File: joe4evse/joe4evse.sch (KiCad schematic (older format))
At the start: 39 parts, among them J1 USB_B_Micro, J10 Conn_01x02, J11 Conn_01x02, J2 Conn_01x03, J3 Conn_01x03, J4 Conn_01x02, J5 Conn_01x03, J6 CONNFLY_Elec_DS1129-04-S8B0P-X, J7 8P8C_LED_Shielded, J9 Conn_01x02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

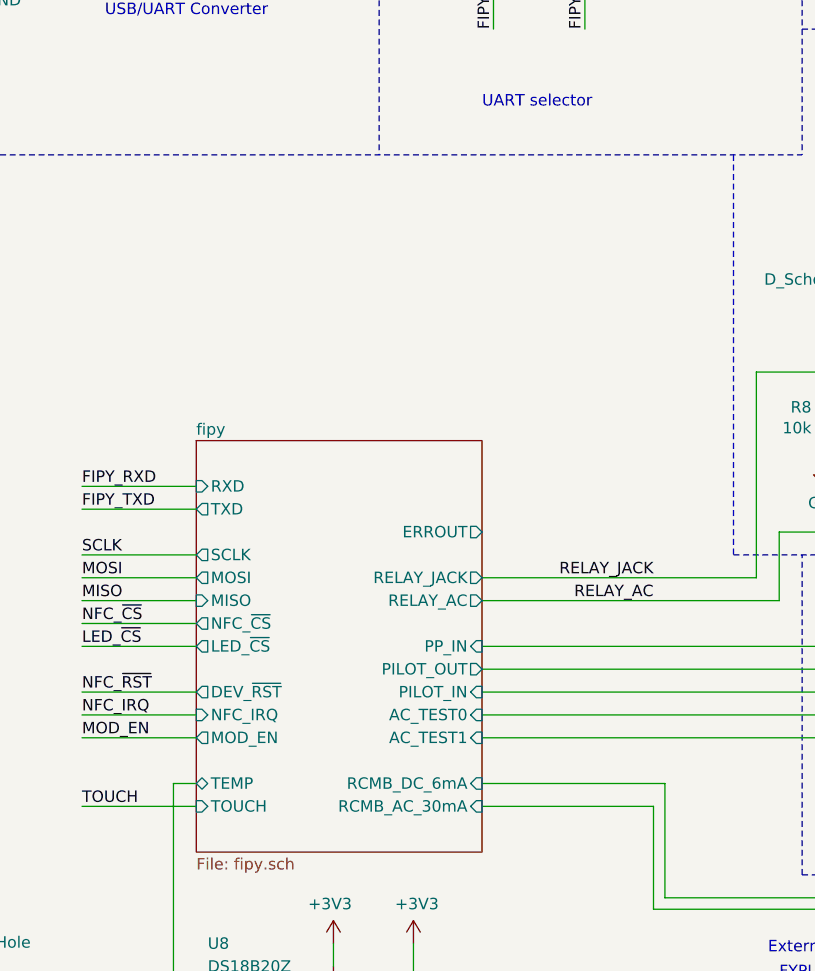
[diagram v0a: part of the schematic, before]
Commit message: joe/*: Add 0.1" header for easy access to RJ45 signals
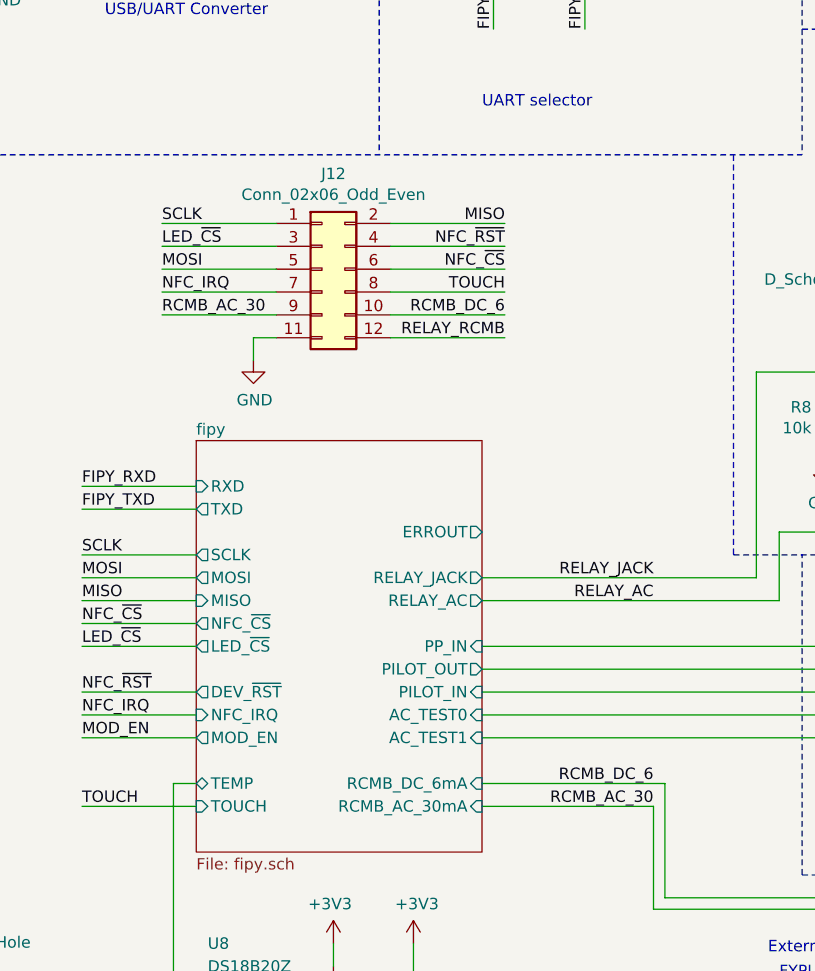
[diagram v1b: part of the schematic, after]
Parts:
- added J12: Conn_02x06_Odd_Even, Connector_PinHeader_2.54mm:PinHeader_2x06_P2.54mm_Vertical, symbol Connector_Generic:Conn_02x06_Odd_Even
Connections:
- net GND: now also J12.11 (Pin_11)
- net LED_~CS: now also J12.3 (Pin_3)
- net MISO: now also J12.2 (Pin_2)
- net MOSI: now also J12.5 (Pin_5)
- net NFC_IRQ: now also J12.7 (Pin_7)
- net NFC_~CS: now also J12.6 (Pin_6)
- net NFC_~RST: now also J12.4 (Pin_4)
- net RELAY_RCMB: now also J12.12 (Pin_12)
- net SCLK: now also J12.1 (Pin_1)
- net TOUCH: now also J12.8 (Pin_8)
- net fipy/RCMB_AC_30mA renamed RCMB_AC_30
- net RCMB_AC_30: now also J12.9 (Pin_9)
- net fipy/RCMB_DC_6mA renamed RCMB_DC_6
- net RCMB_DC_6: now also J12.10 (Pin_10)
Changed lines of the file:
@@
 Wire Wire Line
 	5450 7100 5450 7400
+$Comp
+L Connector_Generic:Conn_02x06_Odd_Even J12
+U 1 1 5DFFDDFE
+P 5050 3650
+F 0 "J12" H 5100 4067 50  0000 C CNN
+F 1 "Conn_02x06_Odd_Even" H 5100 3976 50  0000 C CNN
+F 2 "Connector_PinHeader_2.54mm:PinHeader_2x06_P2.54mm_Vertical" H 5050 3650 50  0001 C CNN
+F 3 "~" H 5050 3650 50  0001 C CNN
+	1    5050 3650
+	1    0    0    -1
+$EndComp
+Wire Wire Line
+	4850 3750 4350 3750
+Wire Wire Line
+	5350 3550 5850 3550
+Wire Wire Line
+	4850 3550 4350 3550
+Wire Wire Line
+	5350 3650 5850 3650
+Wire Wire Line
+	4850 3650 4350 3650
+Wire Wire Line
+	5350 3450 5850 3450
+Wire Wire Line
+	4850 3450 4350 3450
+Text Label 4350 3450 0    50   ~ 0
+SCLK
+Text Label 5850 3450 2    50   ~ 0
+MISO
+Text Label 4350 3650 0    50   ~ 0
+MOSI
+Text Label 5850 3650 2    50   ~ 0
+NFC_~CS
+Text Label 4350 3550 0    50   ~ 0
+LED_~CS
+Text Label 5850 3550 2    50   ~ 0
+NFC_~RST
+Text Label 4350 3750 0    50   ~ 0
+NFC_IRQ
+Text Label 5850 3750 2    50   ~ 0
+TOUCH
+Wire Wire Line
+	5350 3750 5850 3750
+Text Label 6500 6000 2    50   ~ 0
+RCMB_AC_30
+Text Label 6500 5900 2    50   ~ 0
+RCMB_DC_6
+Wire Wire Line
+	4850 3850 4350 3850
+Wire Wire Line
+	5350 3850 5850 3850
+Text Label 4350 3850 0    50   ~ 0
+RCMB_AC_30
+Text Label 5850 3850 2    50   ~ 0
+RCMB_DC_6
+Text Label 5850 3950 2    50   ~ 0
+RELAY_RCMB
+Wire Wire Line
+	5850 3950 5350 3950
+$Comp
+L power:GND #PWR075
+U 1 1 5E0BB16B
+P 4750 4050
+AR Path="/5E0BB16B" Ref="#PWR075"  Part="1"
+AR Path="/5E295EB5/5E0BB16B" Ref="#PWR?"  Part="1"
+AR Path="/5E2A129E/5E0BB16B" Ref="#PWR?"  Part="1"
+AR Path="/5E2A9DD8/5E0BB16B" Ref="#PWR?"  Part="1"
+F 0 "#PWR075" H 4750 3800 50  0001 C CNN
+F 1 "GND" H 4755 3877 50  0000 C CNN
+F 2 "" H 4750 4050 50  0001 C CNN
+F 3 "" H 4750 4050 50  0001 C CNN
+	1    4750 4050
+	1    0    0    -1
+$EndComp
+Wire Wire Line
+	4750 4050 4750 3950
+Wire Wire Line
+	4750 3950 4850 3950
 $EndSCHEMATC

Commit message: joe/pcb: Misc silk fixes
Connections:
- net MOD_A: now reaches J2.3 (Pin_3), U2.6 (A)
- net MOD_B: now reaches J2.1 (Pin_1), U2.7 (B)
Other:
- moved on the sheet: J2
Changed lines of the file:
@@
 L power:GND #PWR014
 U 1 1 5D2C078F
-P 9650 2300
-F 0 "#PWR014" H 9650 2050 50  0001 C CNN
-F 1 "GND" H 9655 2127 50  0000 C CNN
-F 2 "" H 9650 2300 50  0001 C CNN
-F 3 "" H 9650 2300 50  0001 C CNN
-	1    9650 2300
+P 9900 2300
+F 0 "#PWR014" H 9900 2050 50  0001 C CNN
+F 1 "GND" H 9905 2127 50  0000 C CNN
+F 2 "" H 9900 2300 50  0001 C CNN
+F 3 "" H 9900 2300 50  0001 C CNN
+	1    9900 2300
 	1    0    0    -1
 $EndComp
@@
 	9550 1800 9550 1750
 Wire Wire Line
-	9550 1750 9750 1750
+	9550 1750 10000 1750
 Wire Wire Line
 	9450 1500 9550 1500
@@
 	9550 1500 9550 1550
 Wire Wire Line
-	9550 1550 9750 1550
-Wire Wire Line
-	9650 2300 9650 1650
-Wire Wire Line
-	9650 1650 9750 1650
+	9550 1550 10000 1550
 $Comp
 L power:+3V3 #PWR03
@@
 Text Label 6300 950  3    50   ~ 0
 MOD_RX
-$Comp
-L Connector_Generic:Conn_01x03 J2
-U 1 1 5E290D0B
-P 9950 1650
-F 0 "J2" H 10030 1692 50  0000 L CNN
-F 1 "Conn_01x03" H 10030 1601 50  0000 L CNN
-F 2 "Connector_JST:JST_PH_B3B-PH-K_1x03_P2.00mm_Vertical" H 9950 1650 50  0001 C CNN
-F 3 "~" H 9950 1650 50  0001 C CNN
-	1    9950 1650
-	1    0    0    -1
-$EndComp
 Wire Wire Line
 	8950 4500 8950 4300
@@
 Wire Wire Line
 	4750 3950 4850 3950
+Text Label 9550 1550 0    50   ~ 0
+MOD_B
+Text Label 9550 1750 0    50   ~ 0
+MOD_A
+$Comp
+L Connector_Generic:Conn_01x03 J2
+U 1 1 5E290D0B
+P 10200 1650
+F 0 "J2" H 10280 1692 50  0000 L CNN
+F 1 "Conn_01x03" H 10280 1601 50  0000 L CNN
+F 2 "Connector_JST:JST_PH_B3B-PH-K_1x03_P2.00mm_Vertical" H 10200 1650 50  0001 C CNN
+F 3 "~" H 10200 1650 50  0001 C CNN
+	1    10200 1650
+	1    0    0    -1
+$EndComp
+Wire Wire Line
+	10000 1650 9900 1650
+Wire Wire Line
+	9900 1650 9900 2300
 $EndSCHEMATC

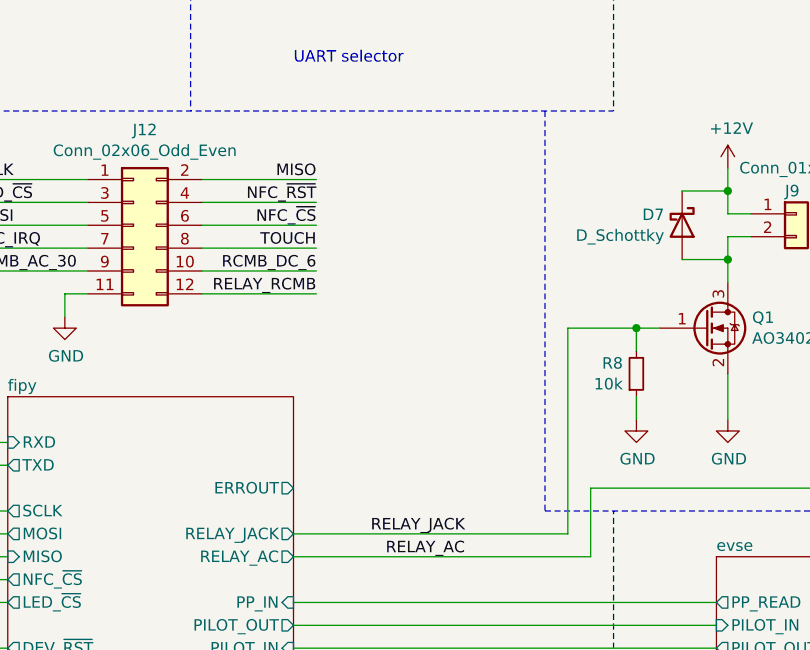
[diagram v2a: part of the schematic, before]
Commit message: joe: Add 12V ERROUT
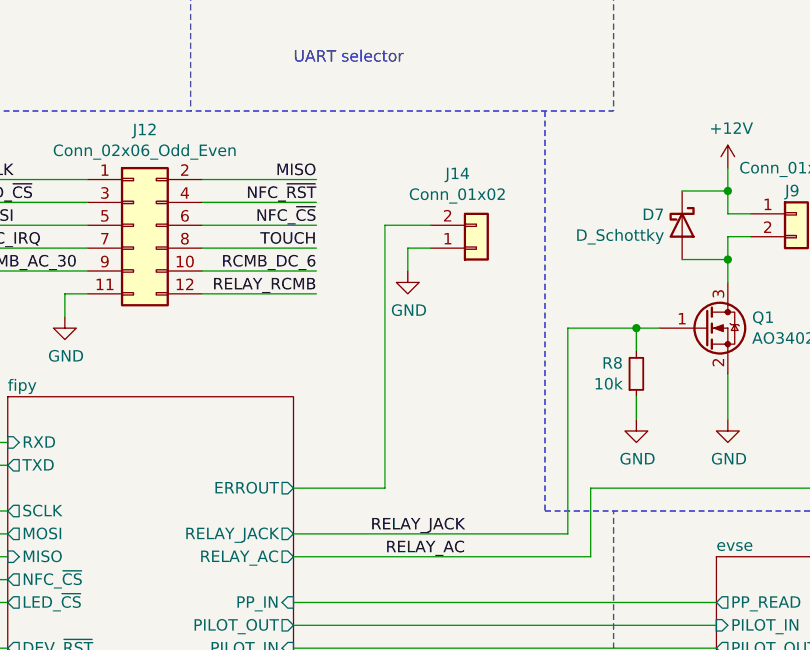
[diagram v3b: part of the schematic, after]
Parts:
- added J14: Conn_01x02, Connector_JST:JST_PH_B2B-PH-K_1x02_P2.00mm_Vertical, symbol Connector_Generic:Conn_01x02
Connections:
- net GND: now also J14.1 (Pin_1)
- net fipy/ERROUT: now also J14.2 (Pin_2)
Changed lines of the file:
@@
 Wire Wire Line
 	5450 7100 5450 7400
-$Comp
-L Connector_Generic:Conn_02x06_Odd_Even J12
-U 1 1 5DFFDDFE
-P 5050 3650
-F 0 "J12" H 5100 4067 50  0000 C CNN
-F 1 "Conn_02x06_Odd_Even" H 5100 3976 50  0000 C CNN
-F 2 "Connector_PinHeader_2.54mm:PinHeader_2x06_P2.54mm_Vertical" H 5050 3650 50  0001 C CNN
-F 3 "~" H 5050 3650 50  0001 C CNN
-	1    5050 3650
-	1    0    0    -1
-$EndComp
-Wire Wire Line
-	4850 3750 4350 3750
-Wire Wire Line
-	5350 3550 5850 3550
-Wire Wire Line
-	4850 3550 4350 3550
-Wire Wire Line
-	5350 3650 5850 3650
-Wire Wire Line
-	4850 3650 4350 3650
-Wire Wire Line
-	5350 3450 5850 3450
-Wire Wire Line
-	4850 3450 4350 3450
-Text Label 4350 3450 0    50   ~ 0
-SCLK
-Text Label 5850 3450 2    50   ~ 0
-MISO
-Text Label 4350 3650 0    50   ~ 0
-MOSI
-Text Label 5850 3650 2    50   ~ 0
-NFC_~CS
-Text Label 4350 3550 0    50   ~ 0
-LED_~CS
-Text Label 5850 3550 2    50   ~ 0
-NFC_~RST
-Text Label 4350 3750 0    50   ~ 0
-NFC_IRQ
-Text Label 5850 3750 2    50   ~ 0
-TOUCH
-Wire Wire Line
-	5350 3750 5850 3750
 Text Label 6500 6000 2    50   ~ 0
 RCMB_AC_30
 Text Label 6500 5900 2    50   ~ 0
 RCMB_DC_6
-Wire Wire Line
-	4850 3850 4350 3850
-Wire Wire Line
-	5350 3850 5850 3850
-Text Label 4350 3850 0    50   ~ 0
-RCMB_AC_30
-Text Label 5850 3850 2    50   ~ 0
-RCMB_DC_6
-Text Label 5850 3950 2    50   ~ 0
-RELAY_RCMB
-Wire Wire Line
-	5850 3950 5350 3950
-$Comp
-L power:GND #PWR075
-U 1 1 5E0BB16B
-P 4750 4050
-AR Path="/5E0BB16B" Ref="#PWR075"  Part="1"
-AR Path="/5E295EB5/5E0BB16B" Ref="#PWR?"  Part="1"
-AR Path="/5E2A129E/5E0BB16B" Ref="#PWR?"  Part="1"
-AR Path="/5E2A9DD8/5E0BB16B" Ref="#PWR?"  Part="1"
-F 0 "#PWR075" H 4750 3800 50  0001 C CNN
-F 1 "GND" H 4755 3877 50  0000 C CNN
-F 2 "" H 4750 4050 50  0001 C CNN
-F 3 "" H 4750 4050 50  0001 C CNN
-	1    4750 4050
-	1    0    0    -1
-$EndComp
-Wire Wire Line
-	4750 4050 4750 3950
-Wire Wire Line
-	4750 3950 4850 3950
 Text Label 9550 1550 0    50   ~ 0
 MOD_B
@@
 Wire Wire Line
 	9900 1650 9900 2300
+Wire Wire Line
+	4750 3950 4850 3950
+Wire Wire Line
+	4750 4050 4750 3950
+$Comp
+L power:GND #PWR075
+U 1 1 5E0BB16B
+P 4750 4050
+AR Path="/5E0BB16B" Ref="#PWR075"  Part="1"
+AR Path="/5E295EB5/5E0BB16B" Ref="#PWR?"  Part="1"
+AR Path="/5E2A129E/5E0BB16B" Ref="#PWR?"  Part="1"
+AR Path="/5E2A9DD8/5E0BB16B" Ref="#PWR?"  Part="1"
+F 0 "#PWR075" H 4750 3800 50  0001 C CNN
+F 1 "GND" H 4755 3877 50  0000 C CNN
+F 2 "" H 4750 4050 50  0001 C CNN
+F 3 "" H 4750 4050 50  0001 C CNN
+	1    4750 4050
+	1    0    0    -1
+$EndComp
+Wire Wire Line
+	5850 3950 5350 3950
+Text Label 5850 3950 2    50   ~ 0
+RELAY_RCMB
+Text Label 5850 3850 2    50   ~ 0
+RCMB_DC_6
+Text Label 4350 3850 0    50   ~ 0
+RCMB_AC_30
+Wire Wire Line
+	5350 3850 5850 3850
+Wire Wire Line
+	4850 3850 4350 3850
+Wire Wire Line
+	5350 3750 5850 3750
+Text Label 5850 3750 2    50   ~ 0
+TOUCH
+Text Label 4350 3750 0    50   ~ 0
+NFC_IRQ
+Text Label 5850 3550 2    50   ~ 0
+NFC_~RST
+Text Label 4350 3550 0    50   ~ 0
+LED_~CS
+Text Label 5850 3650 2    50   ~ 0
+NFC_~CS
+Text Label 4350 3650 0    50   ~ 0
+MOSI
+Text Label 5850 3450 2    50   ~ 0
+MISO
+Text Label 4350 3450 0    50   ~ 0
+SCLK
+Wire Wire Line
+	4850 3450 4350 3450
+Wire Wire Line
+	5350 3450 5850 3450
+Wire Wire Line
+	4850 3650 4350 3650
+Wire Wire Line
+	5350 3650 5850 3650
+Wire Wire Line
+	4850 3550 4350 3550
+Wire Wire Line
+	5350 3550 5850 3550
+Wire Wire Line
+	4850 3750 4350 3750
+$Comp
+L Connector_Generic:Conn_02x06_Odd_Even J12
+U 1 1 5DFFDDFE
+P 5050 3650
+F 0 "J12" H 5100 4067 50  0000 C CNN
+F 1 "Conn_02x06_Odd_Even" H 5100 3976 50  0000 C CNN
+F 2 "Connector_PinHeader_2.54mm:PinHeader_2x06_P2.54mm_Vertical" H 5050 3650 50  0001 C CNN
+F 3 "~" H 5050 3650 50  0001 C CNN
+	1    5050 3650
+	1    0    0    -1
+$EndComp
+$Comp
+L Connector_Generic:Conn_01x02 J14
+U 1 1 5E66DC84
+P 6550 3750
+F 0 "J14" H 6468 3425 50  0000 C CNN
+F 1 "Conn_01x02" H 6468 3516 50  0000 C CNN
+F 2 "Connector_JST:JST_PH_B2B-PH-K_1x02_P2.00mm_Vertical" H 6550 3750 50  0001 C CNN
+F 3 "~" H 6550 3750 50  0001 C CNN
+	1    6550 3750
+	1    0    0    1
+$EndComp
+$Comp
+L power:GND #PWR081
+U 1 1 5E66E81F
+P 6250 3850
+AR Path="/5E66E81F" Ref="#PWR081"  Part="1"
+AR Path="/5E295EB5/5E66E81F" Ref="#PWR?"  Part="1"
+AR Path="/5E2A129E/5E66E81F" Ref="#PWR?"  Part="1"
+AR Path="/5E2A9DD8/5E66E81F" Ref="#PWR?"  Part="1"
+F 0 "#PWR081" H 6250 3600 50  0001 C CNN
+F 1 "GND" H 6255 3677 50  0000 C CNN
+F 2 "" H 6250 3850 50  0001 C CNN
+F 3 "" H 6250 3850 50  0001 C CNN
+	1    6250 3850
+	1    0    0    -1
+$EndComp
+Wire Wire Line
+	6250 3850 6250 3750
+Wire Wire Line
+	6250 3750 6350 3750
+Wire Wire Line
+	5750 4800 6150 4800
+Wire Wire Line
+	6150 4800 6150 3650
+Wire Wire Line
+	6150 3650 6350 3650
 $EndSCHEMATC

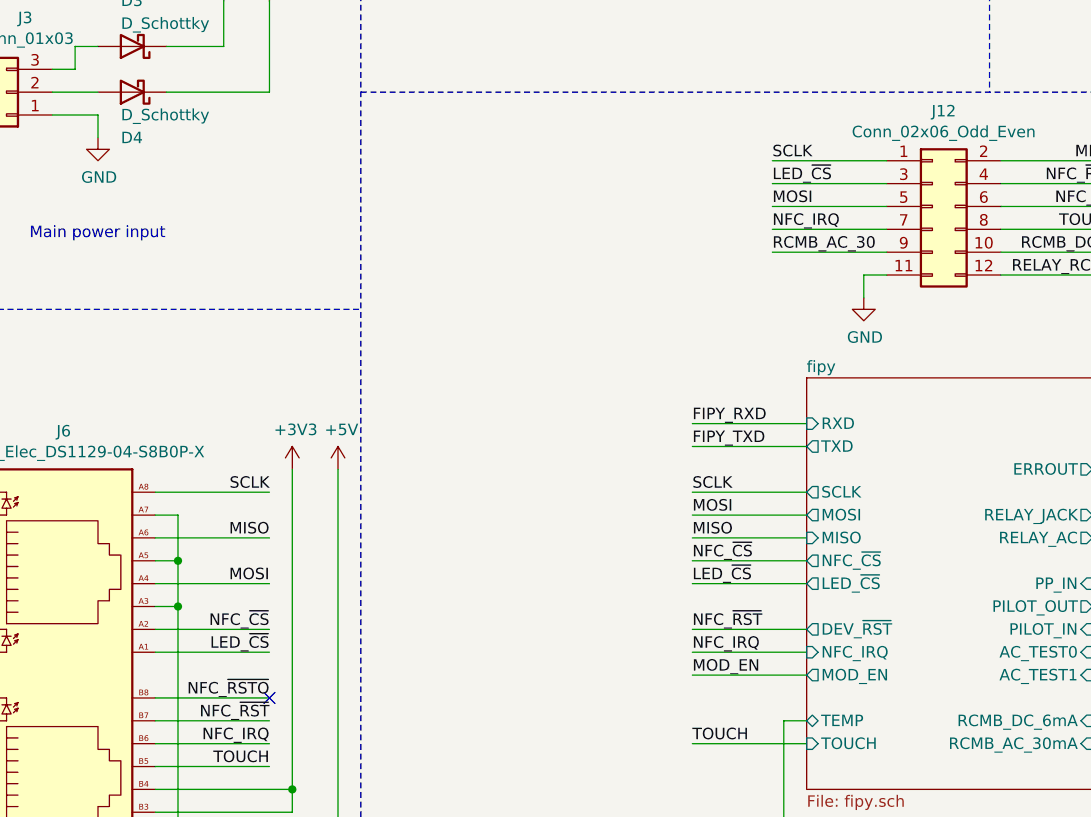
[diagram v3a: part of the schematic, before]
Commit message: joe/*: Rename LED_CS signal to LED_LAT
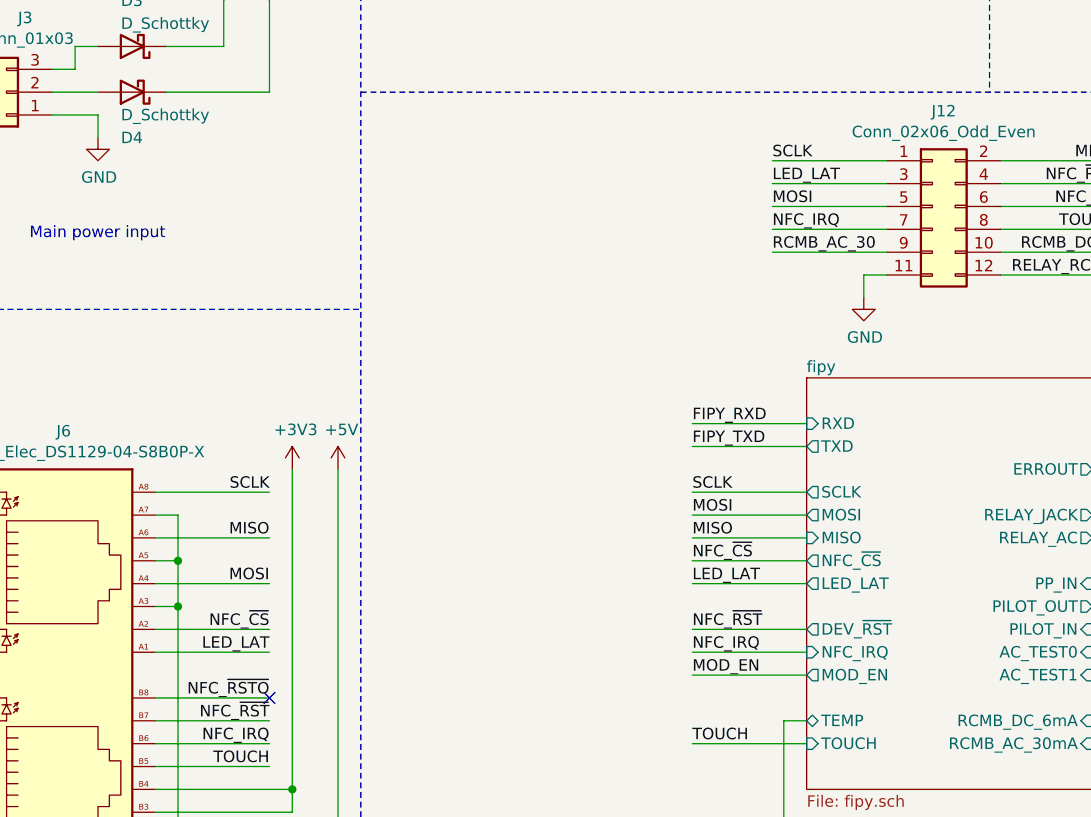
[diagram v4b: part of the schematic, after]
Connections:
- net LED_~CS renamed LED_LAT
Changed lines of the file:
@@
 F6 "MISO" I L 4500 5100 50
 F7 "NFC_~CS" O L 4500 5200 50
-F8 "LED_~CS" O L 4500 5300 50
+F8 "LED_LAT" O L 4500 5300 50
 F9 "DEV_~RST" O L 4500 5500 50
 F10 "NFC_IRQ" I L 4500 5600 50
@@
 NFC_~CS
 Text Label 2150 5600 2    50   ~ 0
-LED_~CS
+LED_LAT
 Text Label 2150 5800 2    50   ~ 0
 NFC_~RSTO
@@
 NFC_~CS
 Text Label 4000 5300 0    50   ~ 0
-LED_~CS
+LED_LAT
 Text Label 4000 5500 0    50   ~ 0
 NFC_~RST
@@
 NFC_~RST
 Text Label 4350 3550 0    50   ~ 0
-LED_~CS
+LED_LAT
 Text Label 5850 3650 2    50   ~ 0
 NFC_~CS
